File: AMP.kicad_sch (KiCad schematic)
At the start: 62 parts, among them Q1 IRF9610PBF, Q11 BCP56-16,115, Q12 BCP56-16,115, Q2 IRF9610PBF, Q3 IRF9610PBF, Q4 IRFP240PBF, Q5 IRFP240PBF, Q6 IRFP240PBF, Q7 IRFP240PBF, Q8 IRFP240PBF, Q9 IRFP240PBF

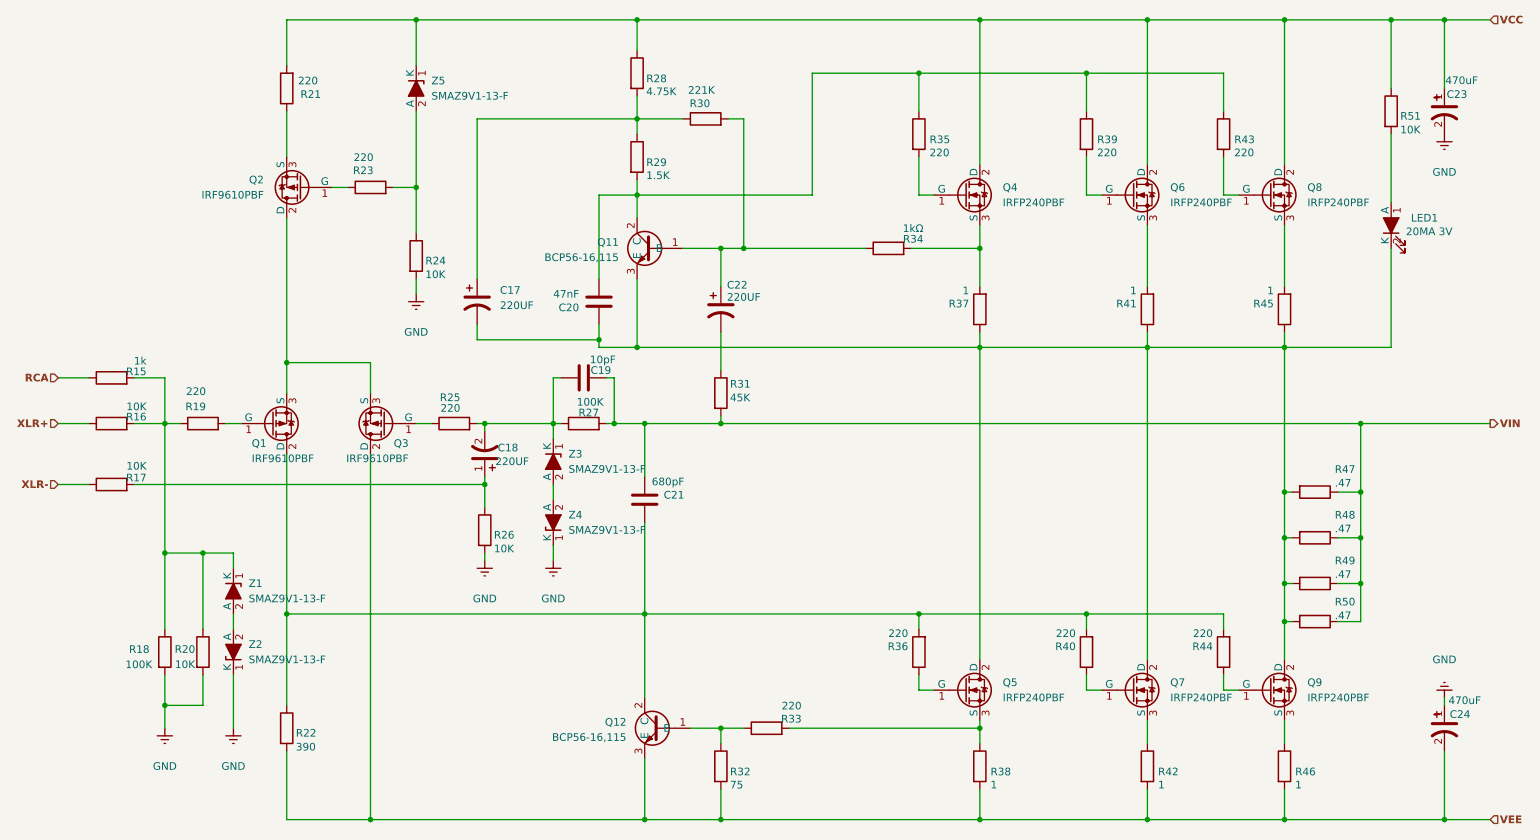
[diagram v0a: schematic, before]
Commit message: using SMD power resistor
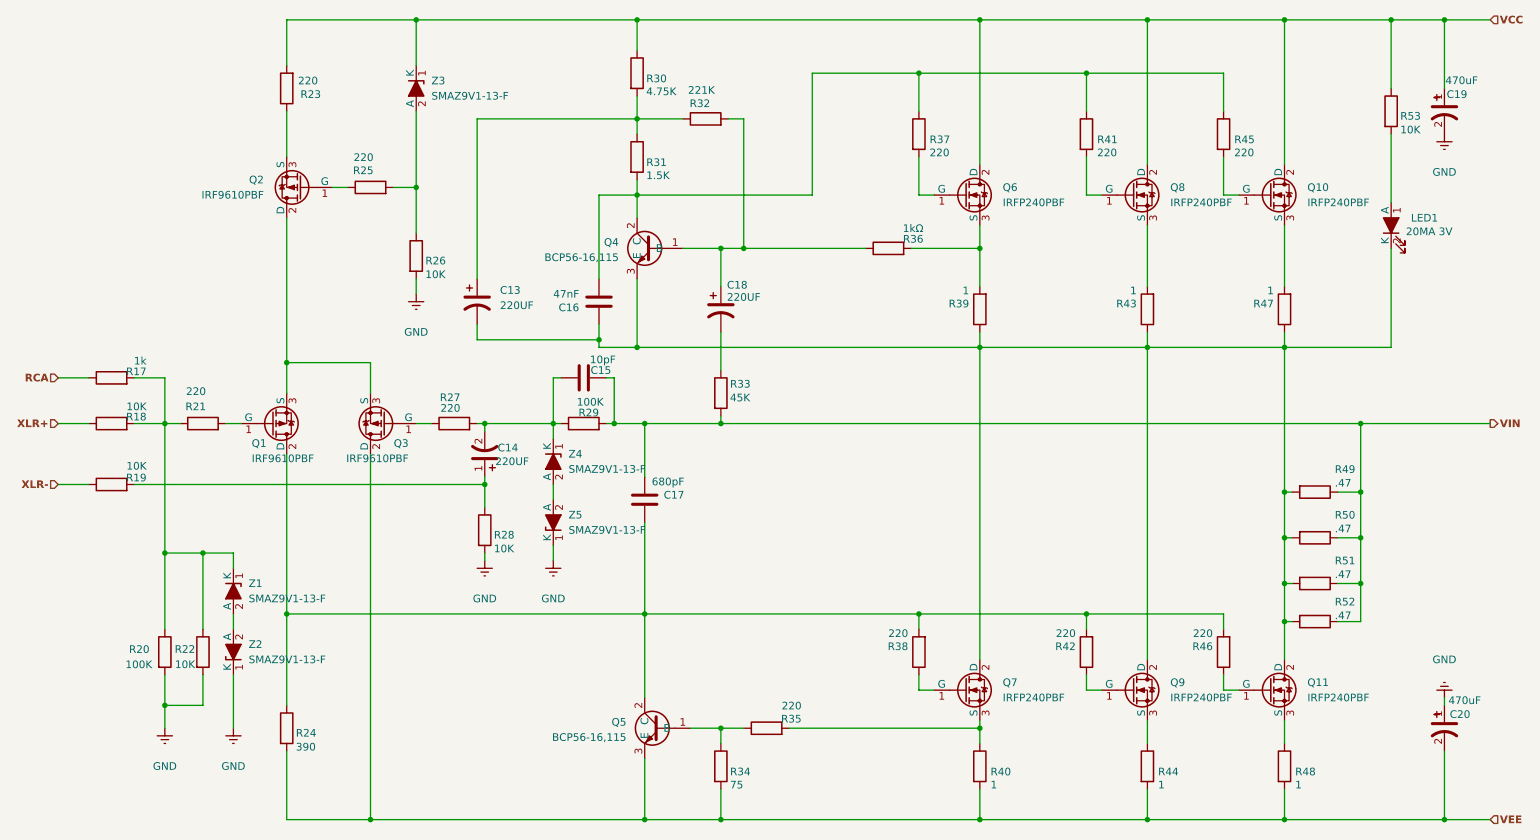
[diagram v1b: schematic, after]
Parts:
- Q10: renamed from Q8; footprint 3rd package:IRFP240PBF -> cus_mosfet:IRFP240PBF
- Q11: renamed from Q9; footprint 3rd package:IRFP240PBF -> cus_mosfet:IRFP240PBF
- Q6: renamed from Q4; footprint 3rd package:IRFP240PBF -> cus_mosfet:IRFP240PBF
- Q7: renamed from Q5; footprint 3rd package:IRFP240PBF -> cus_mosfet:IRFP240PBF
- Q8: renamed from Q6; footprint 3rd package:IRFP240PBF -> cus_mosfet:IRFP240PBF
- Q9: renamed from Q7; footprint 3rd package:IRFP240PBF -> cus_mosfet:IRFP240PBF
- R39: renamed from R37; footprint generic package:R 10W -> cus_resistor:SMW51R0JT
- R40: renamed from R38; footprint generic package:R 10W -> cus_resistor:SMW51R0JT
- R43: renamed from R41; footprint generic package:R 10W -> cus_resistor:SMW51R0JT
- R44: renamed from R42; footprint generic package:R 10W -> cus_resistor:SMW51R0JT
- R47: renamed from R45; footprint generic package:R 10W -> cus_resistor:SMW51R0JT
- R48: renamed from R46; footprint generic package:R 10W -> cus_resistor:SMW51R0JT
- R49: renamed from R47; footprint generic package:R 10W -> cus_resistor:SMW3R47JT
- R50: renamed from R48; footprint generic package:R 10W -> cus_resistor:SMW3R47JT
- R51: renamed from R49; footprint generic package:R 10W -> cus_resistor:SMW3R47JT
- R52: renamed from R50; footprint generic package:R 10W -> cus_resistor:SMW3R47JT
- renumbered C17 to C13, C18 to C14, C19 to C15, C20 to C16, C21 to C17, C22 to C18, C23 to C19, C24 to C20, Q11 to Q4, Q12 to Q5, R15 to R17, R16 to R18, R17 to R19, R18 to R20, R19 to R21, R20 to R22, R21 to R23, R22 to R24, R23 to R25, R24 to R26, R25 to R27, R26 to R28, R27 to R29, R28 to R30, R29 to R31, R30 to R32, R31 to R33, R32 to R34, R33 to R35, R34 to R36, R35 to R37, R36 to R38, R39 to R41, R40 to R42, R43 to R45, R44 to R46, R51 to R53, Z5 to Z3, Z3 to Z4, Z4 to Z5
